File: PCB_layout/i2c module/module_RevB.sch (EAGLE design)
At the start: 16 parts, among them IC1 ATTINY85-20SU, J1 M20-9980346, P1 PROTO_VIAS_01X01-1.2

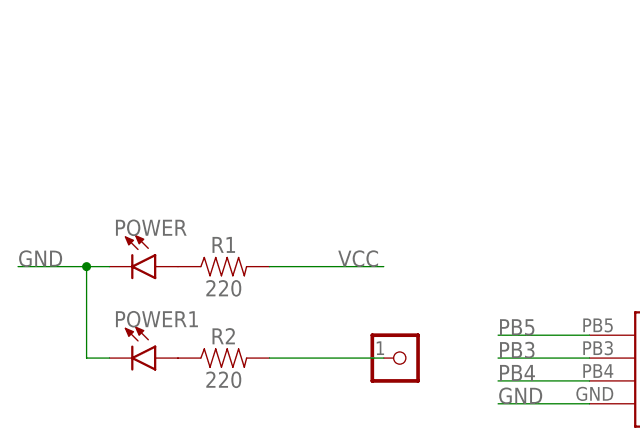
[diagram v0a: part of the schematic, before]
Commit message: added decoupling cap to VCC/GND line
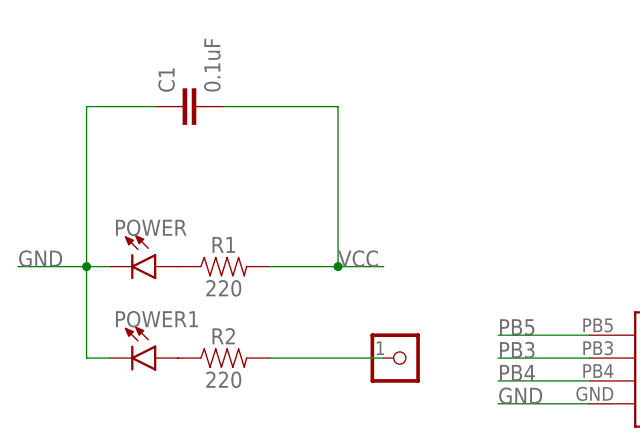
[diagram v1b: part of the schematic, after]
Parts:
- added C1: 0.1uF, SparkFun-Capacitors:0.1UF-0603-25V-5%
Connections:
- net GND: now also C1.1
- net VCC: now also C1.2
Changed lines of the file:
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@@
 <?xml version="1.0" encoding="utf-8"?>
 <!DOCTYPE eagle SYSTEM "eagle.dtd">
-<eagle version="9.0.1">
+<eagle version="9.1.1">
 <drawing>
 <settings>
@@
 <part name="5" library="BadgeParts" deviceset="3X-PADS-CONNECTED" device=""/>
 <part name="J1" library="BadgeParts" deviceset="M20-9980346" device=""/>
+<part name="C1" library="SparkFun-Capacitors" library_urn="urn:adsk.eagle:library:510" deviceset="0.1UF" device="-0603-25V-5%" package3d_urn="urn:adsk.eagle:package:37414/1" value="0.1uF"/>
 </parts>
 <sheets>
@@
 <instance part="5" gate="G$1" x="63.5" y="10.16"/>
 <instance part="J1" gate="G$1" x="-25.4" y="30.48"/>
+<instance part="C1" gate="G$1" x="-38.1" y="81.28" rot="R90"/>
 </instances>
 <busses>
@@
 <pinref part="R1" gate="G$1" pin="2"/>
 <label x="-22.86" y="63.5" size="1.778" layer="95"/>
-<wire x1="-30.48" y1="63.5" x2="-17.78" y2="63.5" width="0.1524" layer="91"/>
+<wire x1="-30.48" y1="63.5" x2="-22.86" y2="63.5" width="0.1524" layer="91"/>
+<pinref part="C1" gate="G$1" pin="2"/>
+<wire x1="-22.86" y1="63.5" x2="-17.78" y2="63.5" width="0.1524" layer="91"/>
+<wire x1="-35.56" y1="81.28" x2="-22.86" y2="81.28" width="0.1524" layer="91"/>
+<wire x1="-22.86" y1="81.28" x2="-22.86" y2="63.5" width="0.1524" layer="91"/>
+<junction x="-22.86" y="63.5"/>
 </segment>
 <segment>
@@
 <wire x1="-50.8" y1="53.34" x2="-50.8" y2="63.5" width="0.1524" layer="91"/>
 <junction x="-50.8" y="63.5"/>
-</segment>
-<segment>
+<pinref part="C1" gate="G$1" pin="1"/>
+<wire x1="-43.18" y1="81.28" x2="-50.8" y2="81.28" width="0.1524" layer="91"/>
+<wire x1="-50.8" y1="81.28" x2="-50.8" y2="63.5" width="0.1524" layer="91"/>
+</segment>
+<segment>

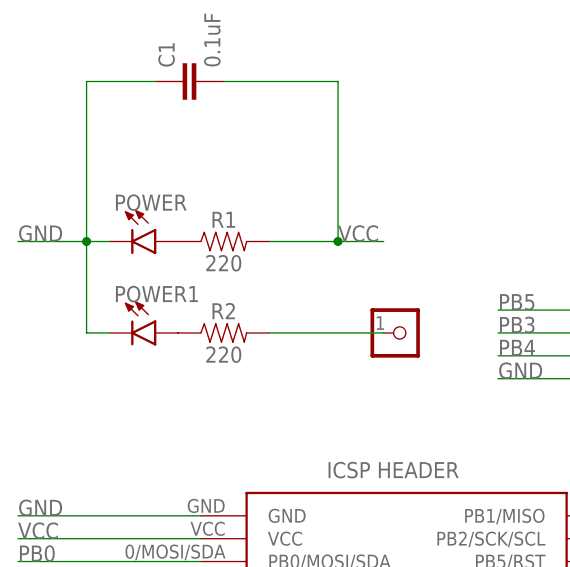
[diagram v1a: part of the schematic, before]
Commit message: updated LED definition
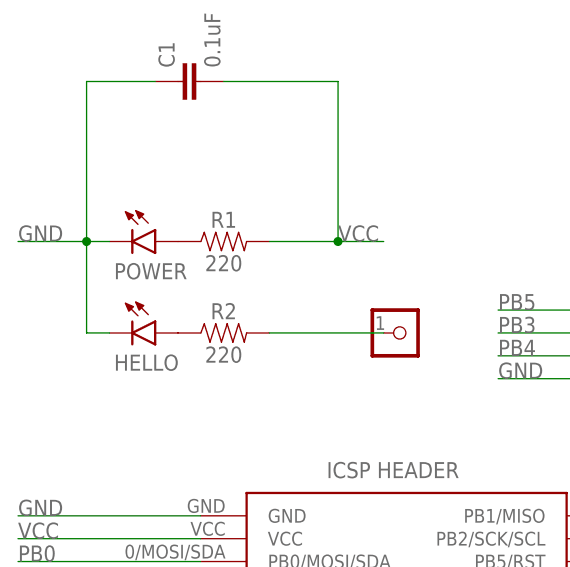
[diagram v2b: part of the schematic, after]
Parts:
- removed POWER1: (no value), SparkFun-LED:LED3MM
- added HELLO: LED3MM, BadgeParts:LED3MM
- POWER: value (none) -> LED3MM; device SparkFun-LED:LED3MM -> BadgeParts:LED3MM
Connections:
- removed net N$11: POWER.A, R1.1
- new net N$3: HELLO.POS, R2.1
- net GND: now also HELLO.NEG, POWER.NEG; no longer POWER.C, POWER1.C
- net N$1: now also POWER.POS, R1.1; no longer POWER1.A, R2.1
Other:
- moved on the sheet: POWER

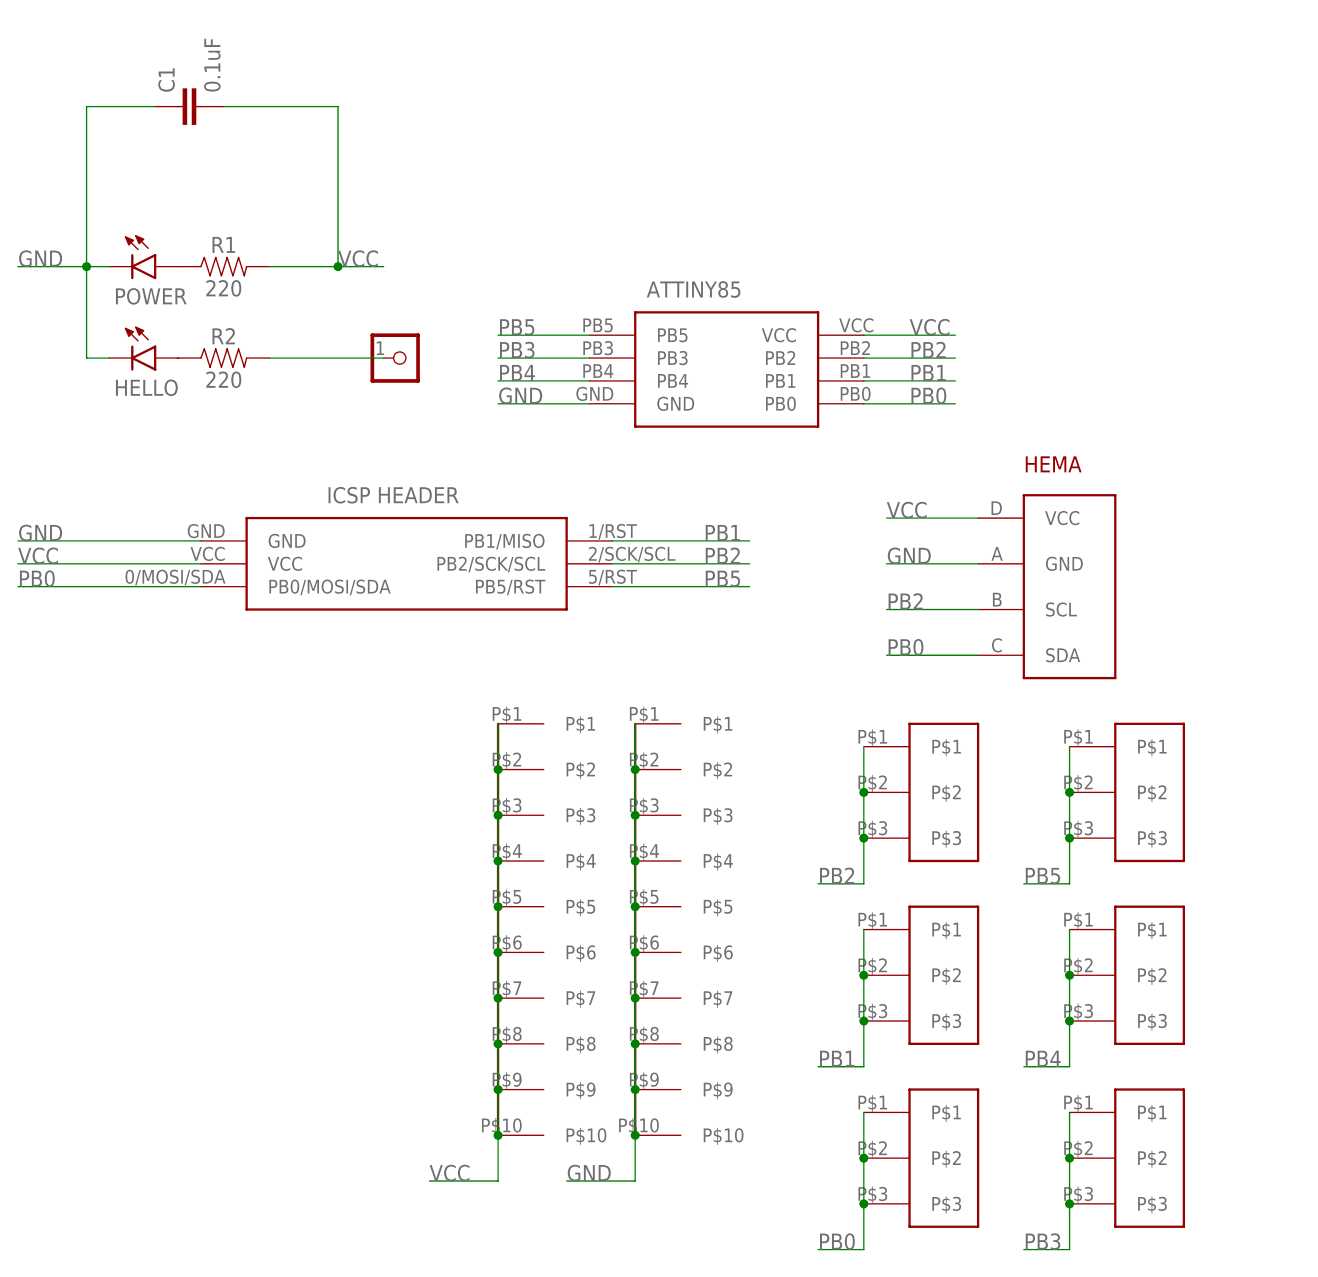
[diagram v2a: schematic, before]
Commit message: swapped hema for 4p header; connect HW to D0, docu
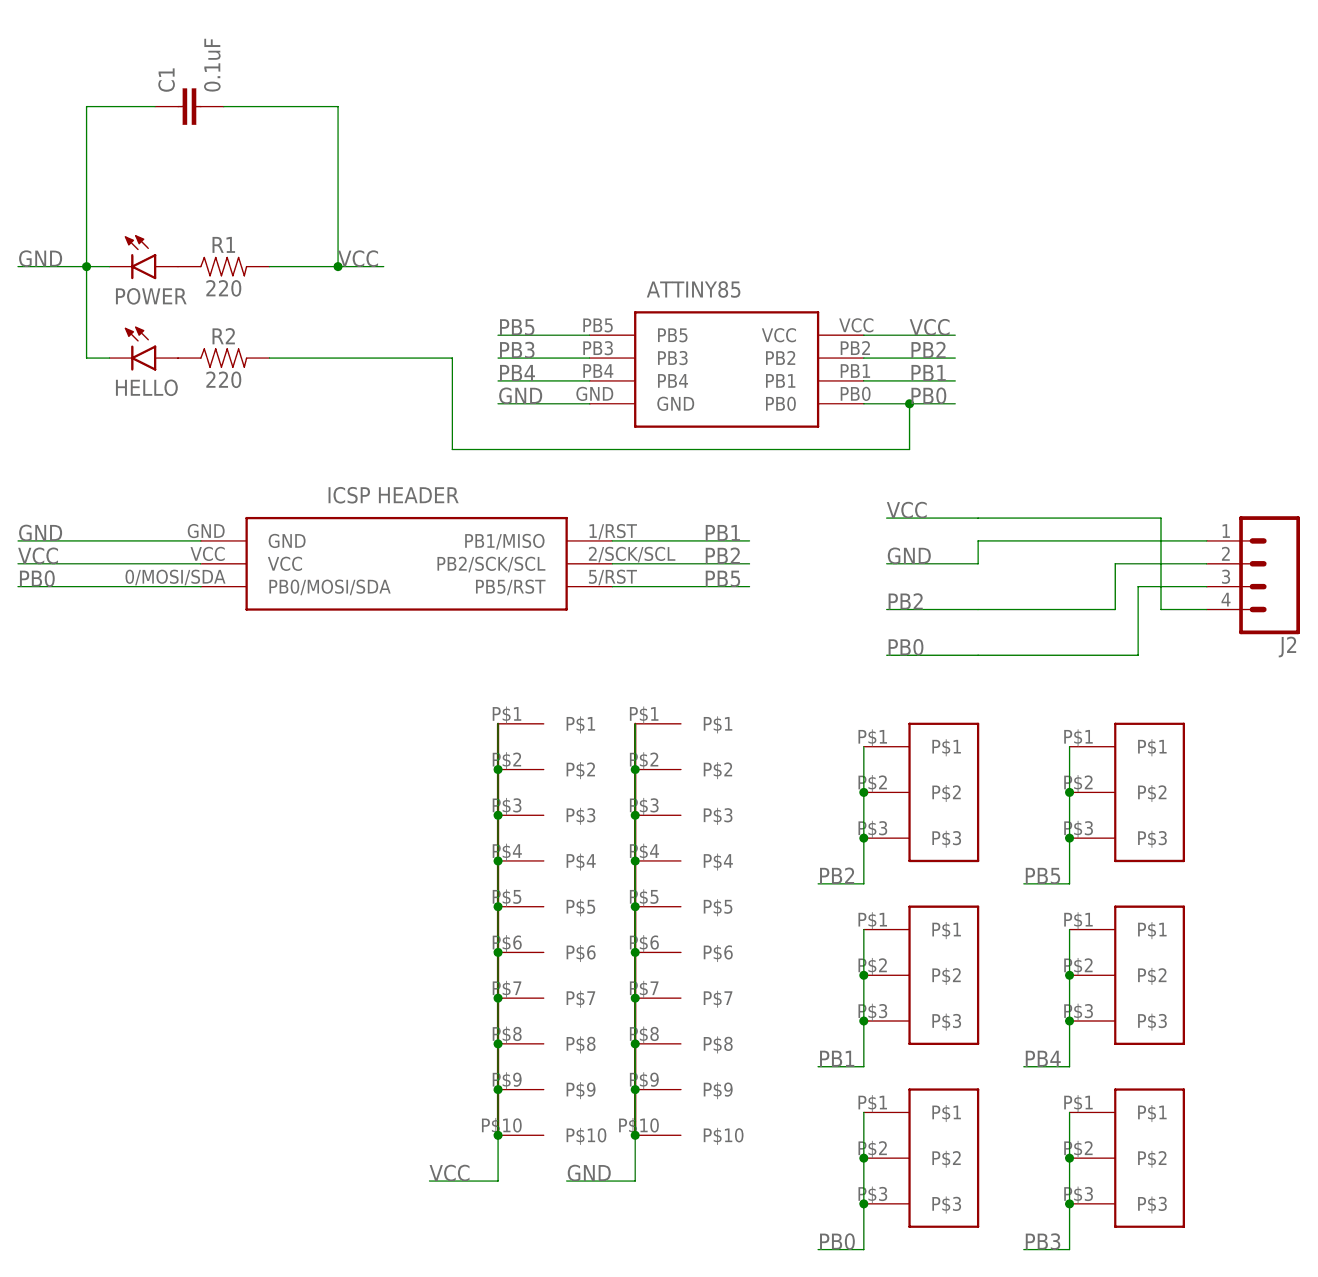
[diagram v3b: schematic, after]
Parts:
- removed P1: PROTO_VIAS_01X01-1.2, dp_devices:PROTO_VIAS_01X01-1.2
- removed U$1: HEMA-I2C, BadgeParts:HEMA-I2C
- added J2: (no value), SparkFun-Connectors:CONN_04
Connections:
- removed net N$2: P1.1, R2.2
- net GND: now also J2.1; no longer U$1.GND
- net PB0: now also J2.3, R2.2; no longer U$1.SDA
- net PB2: now also J2.2; no longer U$1.SCL
- net VCC: now also J2.4; no longer U$1.VCC
